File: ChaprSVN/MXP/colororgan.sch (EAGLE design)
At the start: 42 parts, among them Q1 2N3904, Q2 2N3906, Q3 2N3906, Q4 2N3906, X1 057-034-1, X2 057-034-1

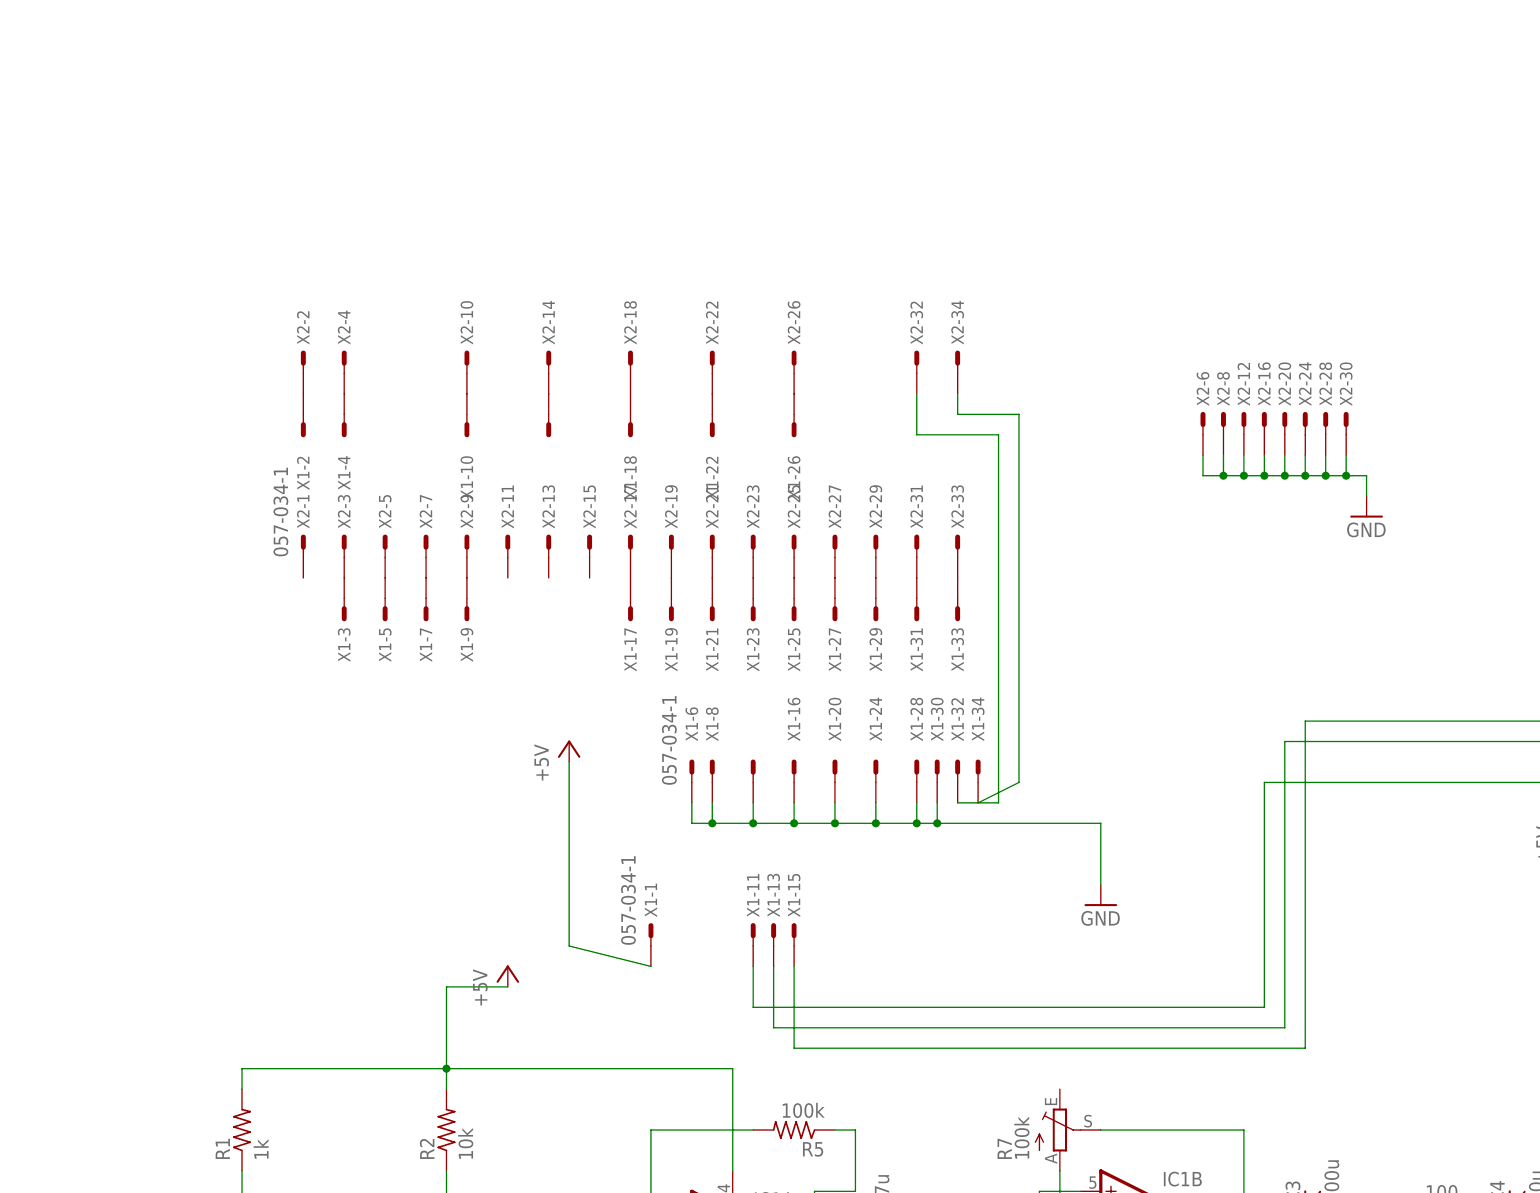
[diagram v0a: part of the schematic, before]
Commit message: A few changes for ease of reading. added 5v to the upward bound MXP connector.
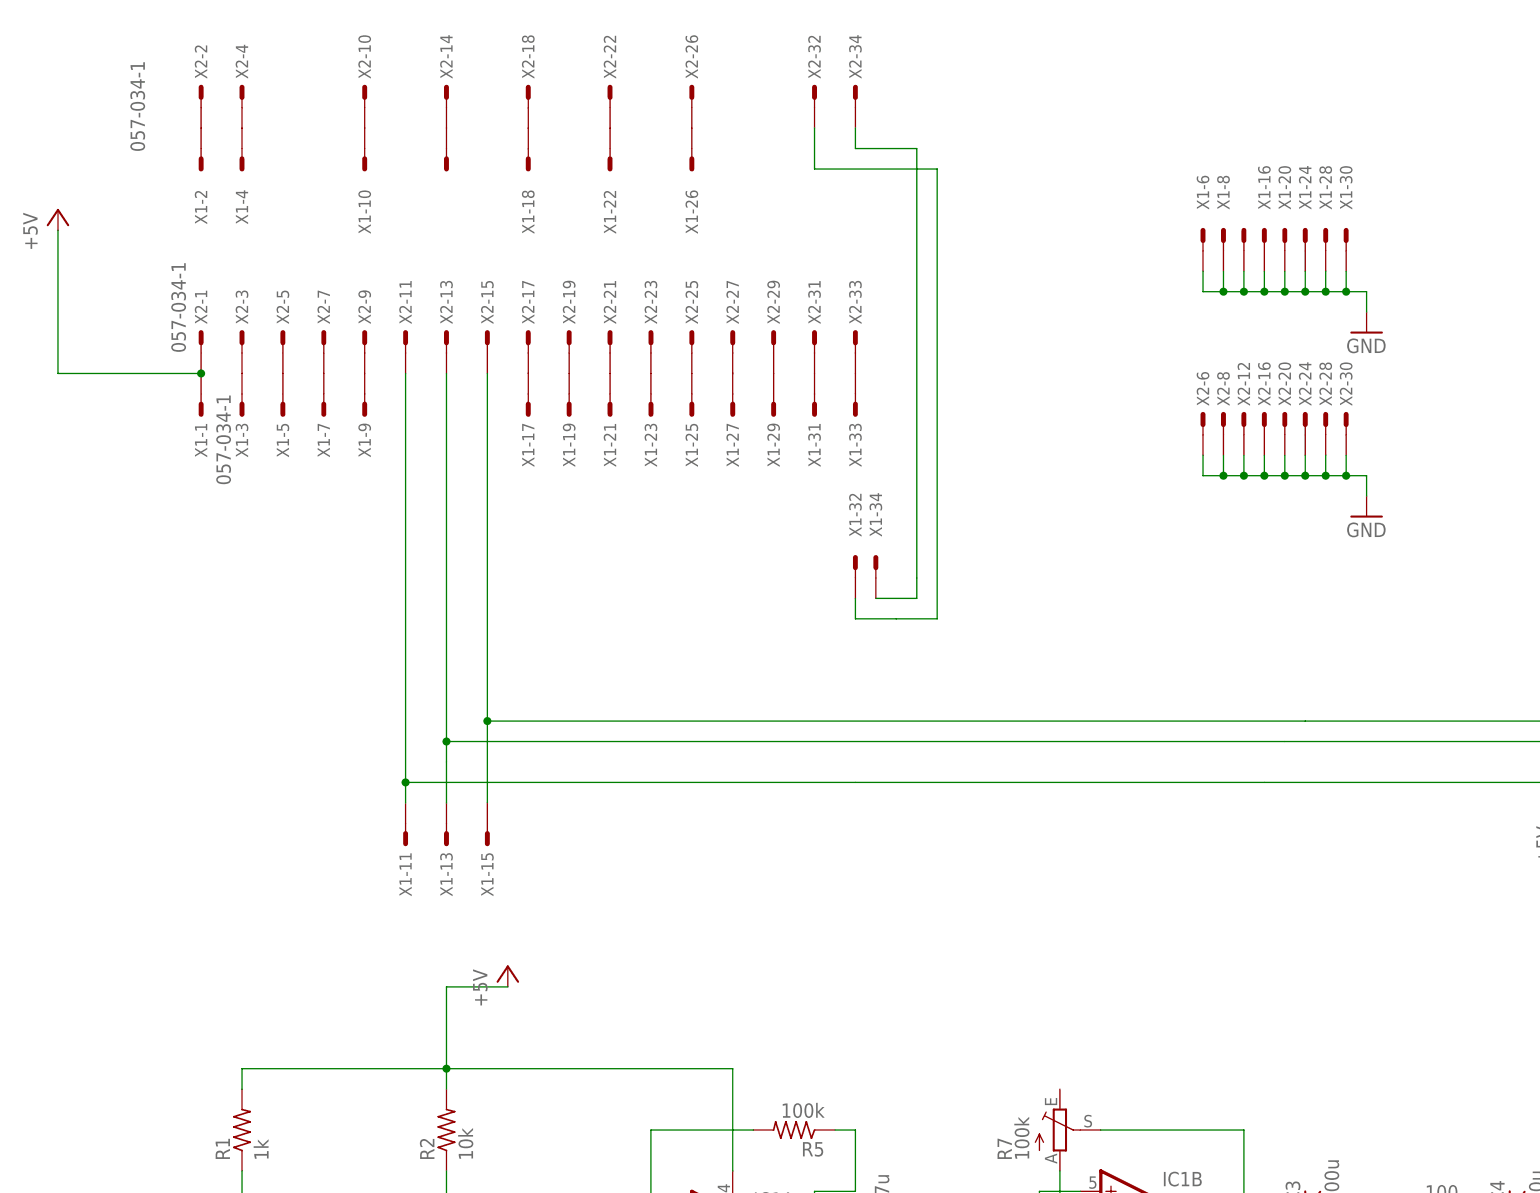
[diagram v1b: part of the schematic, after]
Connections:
- net +5V: now also X2-1.S
- net N$20: now also X2-11.S
- net N$24: now also X2-13.S
- net N$29: now also X2-15.S
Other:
- moved on the sheet: X1-1, X1-10, X1-11, X1-13, X1-15, X1-16, X1-17, X1-18, X1-19, X1-2, X1-20, X1-21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
